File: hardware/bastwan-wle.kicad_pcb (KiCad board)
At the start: 2 copper layers, 50.8 x 22.9 mm, 34 parts, among them J1 USB_B_Micro, J2 Conn_Right, J3 Conn_Left, J4 Conn_Battery, J5 SWD, Q1 DMG3415U-7, U1 RAK3172, U2 AP2112K-3.3TRG1, U3 CP2102N-A01-GQFN28, U5 MCP73831-3-OT

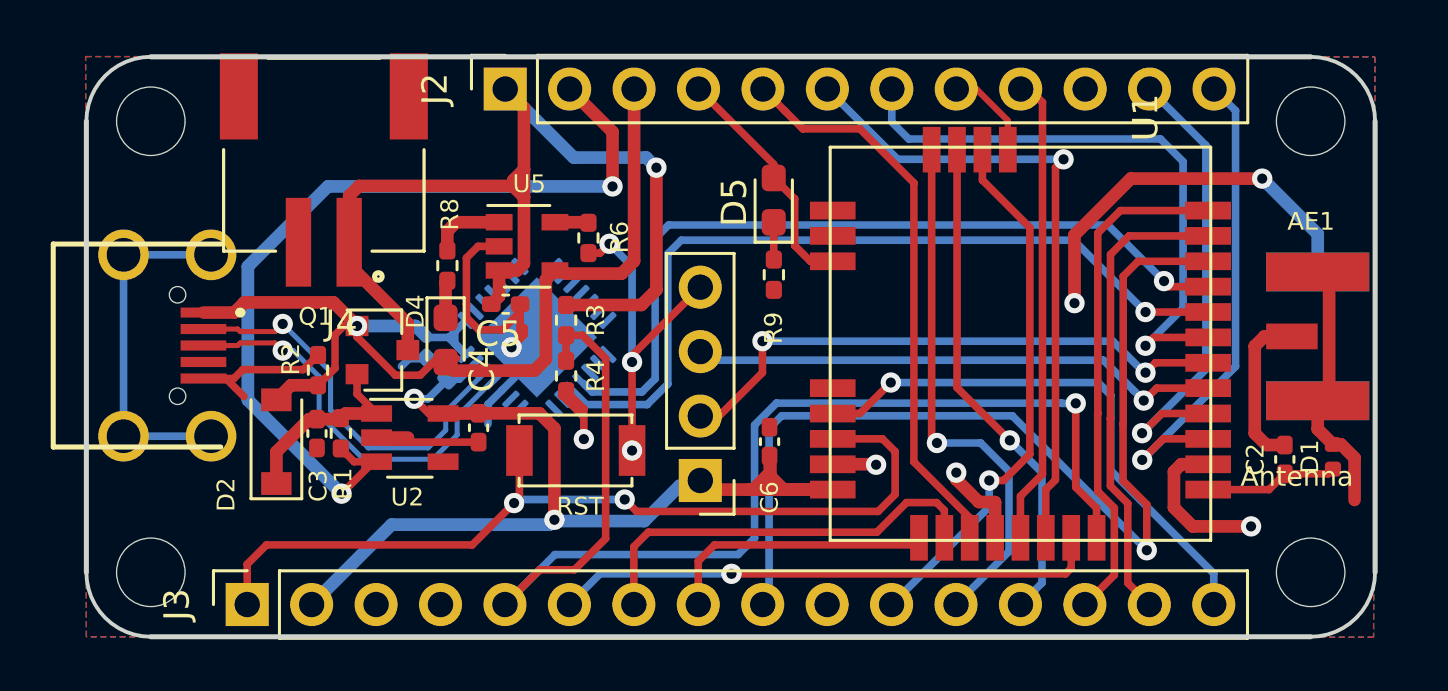
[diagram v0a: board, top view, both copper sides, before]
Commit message: fix labels
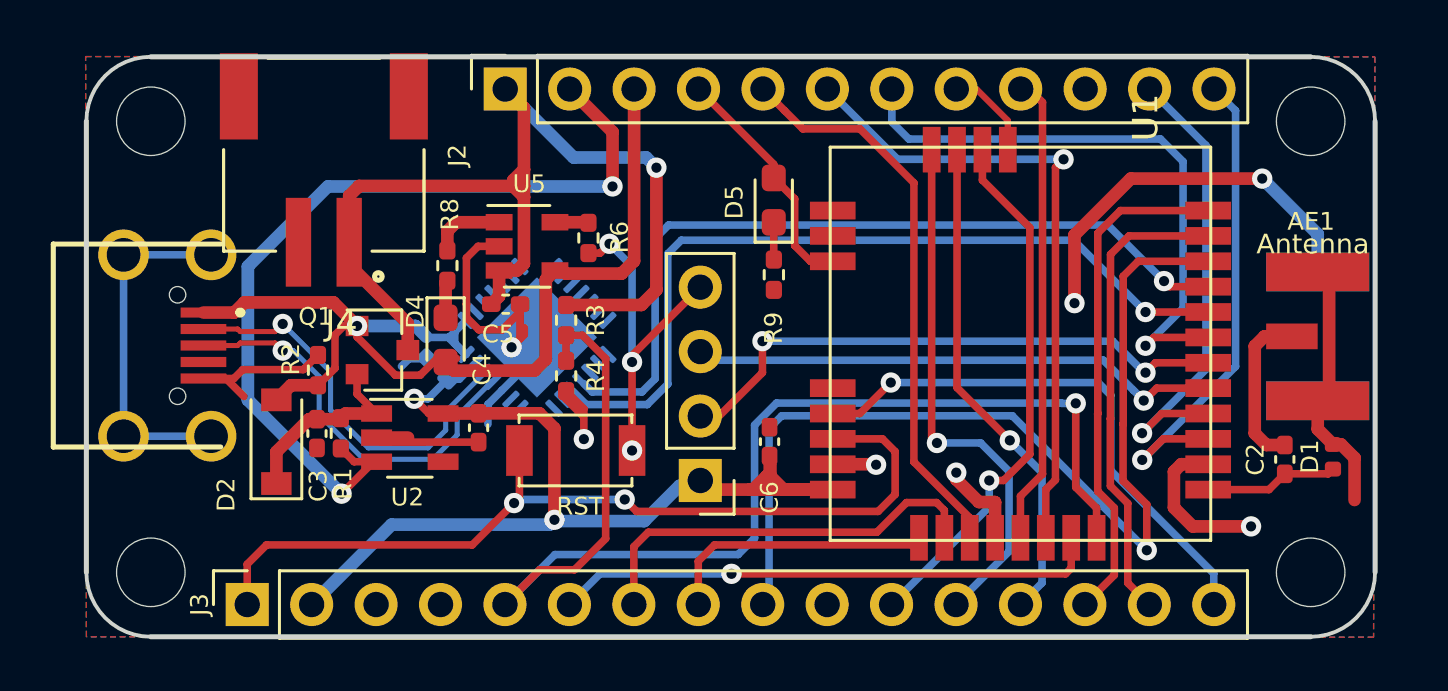
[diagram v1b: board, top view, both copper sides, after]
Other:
- board text added: "CIPO"
- board text added: "CLK"
- board text added: "COPI"
- board text removed: "AREF"
- board text removed: "MISO"
- board text removed: "MOSI"
- board text removed: "SCK"

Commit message: Last_route
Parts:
- removed R1: 100K, Resistor_SMD:R_0402_1005Metric_Pad0.72x0.64mm_HandSolder
- U2: value AP2112K-3.3TRG1 -> MCP1700_DFN6; footprint Package_TO_SOT_SMD:TSOT-23-5 -> Package_DFN_QFN:DFN-6-1EP_2x2mm_P0.65mm_EP1x1.6mm
- moved U2 1.33 mm to (125.3, 77.5)
- moved J4 0.86 mm to (124.1, 69.9)
- moved R3 0.81 mm to (133.6, 73.0)
- moved R4 0.81 mm to (133.6, 75.2)
- renumbered RST to SW1
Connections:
- J2 pad 2: /EN -> Net-(J2-Pad2)
- U2 pad 2: GND -> (no net)
- U2 pad 3: /EN -> GND
- U2 pad 5: +3V3 -> (no net)
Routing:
- net /EN: track 34.2 -> 0.00 mm, vias 2 -> 0
- net GND: track 95.5 -> 89.6 mm, vias 10 -> 16
- net /A0: track 49.1 -> 45.9 mm
- net +BATT: track 41.1 -> 39.0 mm
- net /SCL: track 18.5 -> 20.5 mm
- net /D10: track 23.9 -> 25.3 mm
- net /D6: track 18.6 -> 20.0 mm
- net /D11: track 25.7 -> 26.9 mm
- net Net-(C3-Pad1): track 7.69 -> 6.53 mm
- net +3V3: track 40.4 -> 41.4 mm
- net /SDA: track 19.4 -> 20.5 mm, vias 1 -> 2
- net /A4: track 39.1 -> 40.1 mm
- net /SWCLK: track 20.4 -> 21.1 mm
- net /SWDIO: track 22.2 -> 22.8 mm

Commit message: Add_GND
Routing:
- net GND: track 89.6 -> 84.4 mm, vias 16 -> 36
- net /D-: track 15.8 -> 14.1 mm
- net /D+: track 15.9 -> 14.3 mm
- net /RST: track 35.3 -> 34.2 mm

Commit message: Last_correction
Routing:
- net GND: track 84.4 -> 84.9 mm, vias 36 -> 37
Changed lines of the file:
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@@
     (thickness 1.6)
     (drawings 36)
-    (tracks 506)
+    (tracks 509)
     (zones 0)
     (modules 33)
@@
   (module Rf:RAK3172 (layer F.Cu)
     (at 158.22 66.22 270)
-    (fp_text reference U1 (at -1.17 2.57 90) (layer F.SilkS)
-      (effects (font (size 1 1) (thickness 0.15)))
+    (fp_text reference U1 (at 2.37 -1.62 90) (layer F.SilkS)
+      (effects (font (size 0.7 0.7) (thickness 0.1)))
     )
     (fp_text value RAK3172 (at 0.02 -2.95 90) (layer F.Fab)
@@
     (tags "resistor handsolder")
     (attr smd)
-    (fp_text reference R8 (at -2.02 -0.1 90) (layer F.SilkS)
+    (fp_text reference R8 (at 0.32 1.08 90) (layer F.SilkS)
       (effects (font (size 0.7 0.7) (thickness 0.15)))
     )
@@
   (segment (start 163.04 77.94) (end 163.36 77.94) (width 0.5) (layer F.Cu) (net 2))
   (segment (start 163.89 78.47) (end 163.89 80.13) (width 0.5) (layer F.Cu) (net 2))
-  (segment (start 162.438 69.648) (end 160.94 68.15) (width 0.5) (layer B.Cu) (net 2))
-  (segment (start 162.438 71.14) (end 162.438 69.648) (width 0.5) (layer B.Cu) (net 2))
   (segment (start 131.66 74.427107) (end 130.281142 75.805965) (width 0.3) (layer B.Cu) (net 2))
   (segment (start 131.66 73.72) (end 131.66 74.427107) (width 0.3) (layer B.Cu) (net 2))
@@
   (segment (start 124.28 78.19) (end 123.1025 78.19) (width 0.5) (layer F.Cu) (net 2))
   (via (at 151.65 72.08) (size 0.8) (drill 0.4) (layers F.Cu B.Cu) (net 2))
-  (segment (start 160.94 68.15) (end 160.25 67.46) (width 0.5) (layer B.Cu) (net 2))
-  (segment (start 160.25 67.46) (end 159.84 67.46) (width 0.5) (layer B.Cu) (net 2))
-  (segment (start 151.65 72.08) (end 151.65 70.881458) (width 0.5) (layer F.Cu) (net 2))
-  (segment (start 151.65 70.881458) (end 155.071458 67.46) (width 0.5) (layer F.Cu) (net 2))
-  (segment (start 155.071458 67.46) (end 159.84 67.46) (width 0.5) (layer F.Cu) (net 2))
   (segment (start 158.12 78.72) (end 156.89 78.72) (width 0.25) (layer F.Cu) (net 2))
   (segment (start 156.89 78.72) (end 156.51 79.1) (width 0.25) (layer F.Cu) (net 2))
@@
   (via (at 143.61 72.38) (size 0.8) (drill 0.4) (layers F.Cu B.Cu) (net 2))
   (via (at 144.64 72.38) (size 0.8) (drill 0.4) (layers F.Cu B.Cu) (net 2))
+  (segment (start 155.071458 67.46) (end 159.34 67.46) (width 0.5) (layer F.Cu) (net 2))
+  (segment (start 159.34 67.46) (end 160.05 68.17) (width 0.5) (layer F.Cu) (net 2))
+  (segment (start 151.65 70.881458) (end 155.071458 67.46) (width 0.5) (layer F.Cu) (net 2))
+  (segment (start 151.65 72.08) (end 151.65 70.881458) (width 0.5) (layer F.Cu) (net 2))
+  (segment (start 162 69.21) (end 160.34 69.21) (width 0.5) (layer B.Cu) (net 2))
+  (segment (start 162.438 71.14) (end 162.438 69.648) (width 0.5) (layer B.Cu) (net 2))
+  (segment (start 162.438 69.648) (end 162 69.21) (width 0.5) (layer B.Cu) (net 2))
+  (segment (start 160.05 68.92) (end 160.34 69.21) (width 0.5) (layer F.Cu) (net 2))
+  (segment (start 160.05 68.17) (end 160.05 68.92) (width 0.5) (layer F.Cu) (net 2))
+  (via (at 160.34 69.21) (size 0.8) (drill 0.4) (layers F.Cu B.Cu) (net 2))
   (segment (start 121.39 78.2325) (end 121.39 79.48) (width 0.5) (layer F.Cu) (net 3))
   (segment (start 122.68 76.9425) (end 121.39 78.2325) (width 0.5) (layer F.Cu) (net 3))

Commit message: Last_fix
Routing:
- net GND: track 84.9 -> 87.4 mm, vias 37 -> 38
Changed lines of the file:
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@@
     (thickness 1.6)
     (drawings 36)
-    (tracks 509)
+    (tracks 513)
     (zones 0)
     (modules 33)
@@
   (segment (start 160.05 68.17) (end 160.05 68.92) (width 0.5) (layer F.Cu) (net 2))
   (via (at 160.34 69.21) (size 0.8) (drill 0.4) (layers F.Cu B.Cu) (net 2))
+  (via (at 123.19 73.189999) (size 0.8) (drill 0.4) (layers F.Cu B.Cu) (net 2))
+  (segment (start 123.03 73.349999) (end 123.19 73.189999) (width 0.25) (layer F.Cu) (net 2))
+  (segment (start 123.03 74.4125) (end 123.03 73.349999) (width 0.25) (layer F.Cu) (net 2))
+  (segment (start 123.19 73.189999) (end 124.08 74.079999) (width 0.25) (layer B.Cu) (net 2))
   (segment (start 121.39 78.2325) (end 121.39 79.48) (width 0.5) (layer F.Cu) (net 3))
   (segment (start 122.68 76.9425) (end 121.39 78.2325) (width 0.5) (layer F.Cu) (net 3))

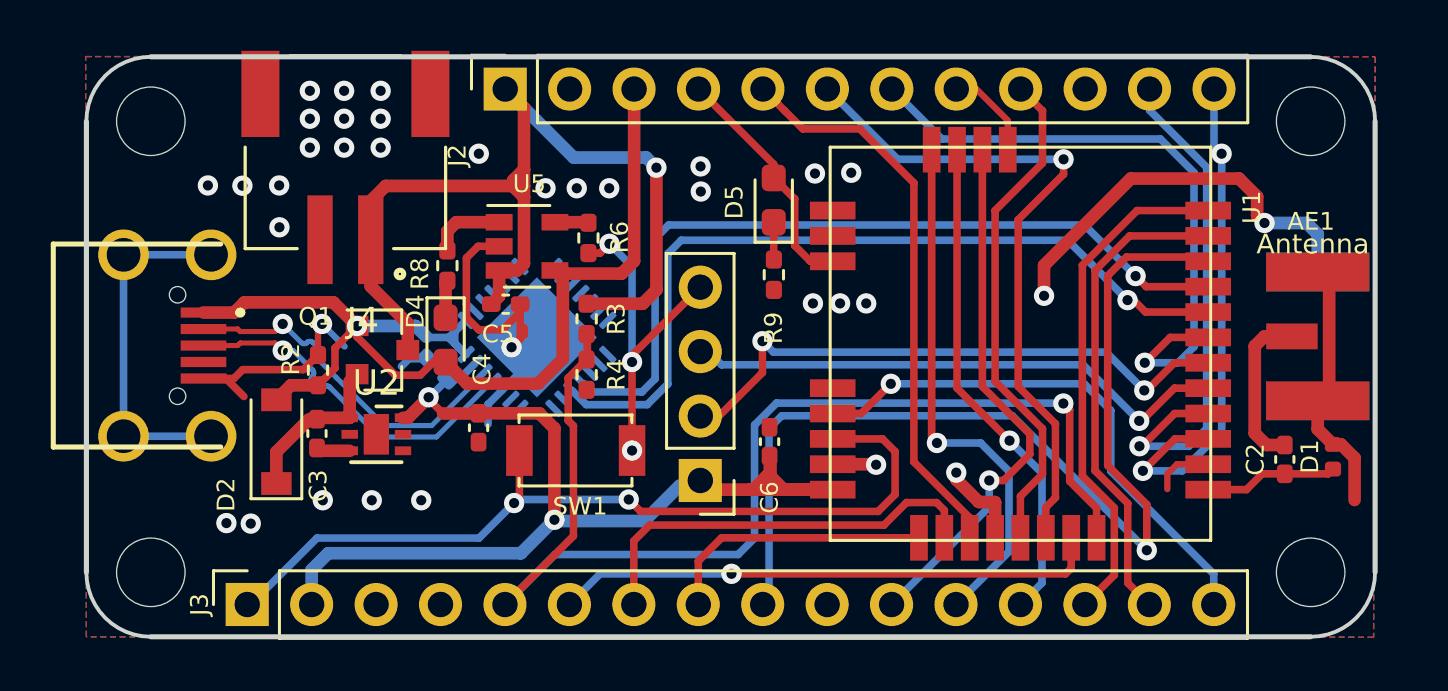
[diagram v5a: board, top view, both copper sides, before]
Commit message: Add_GND_Connection_to_Batt
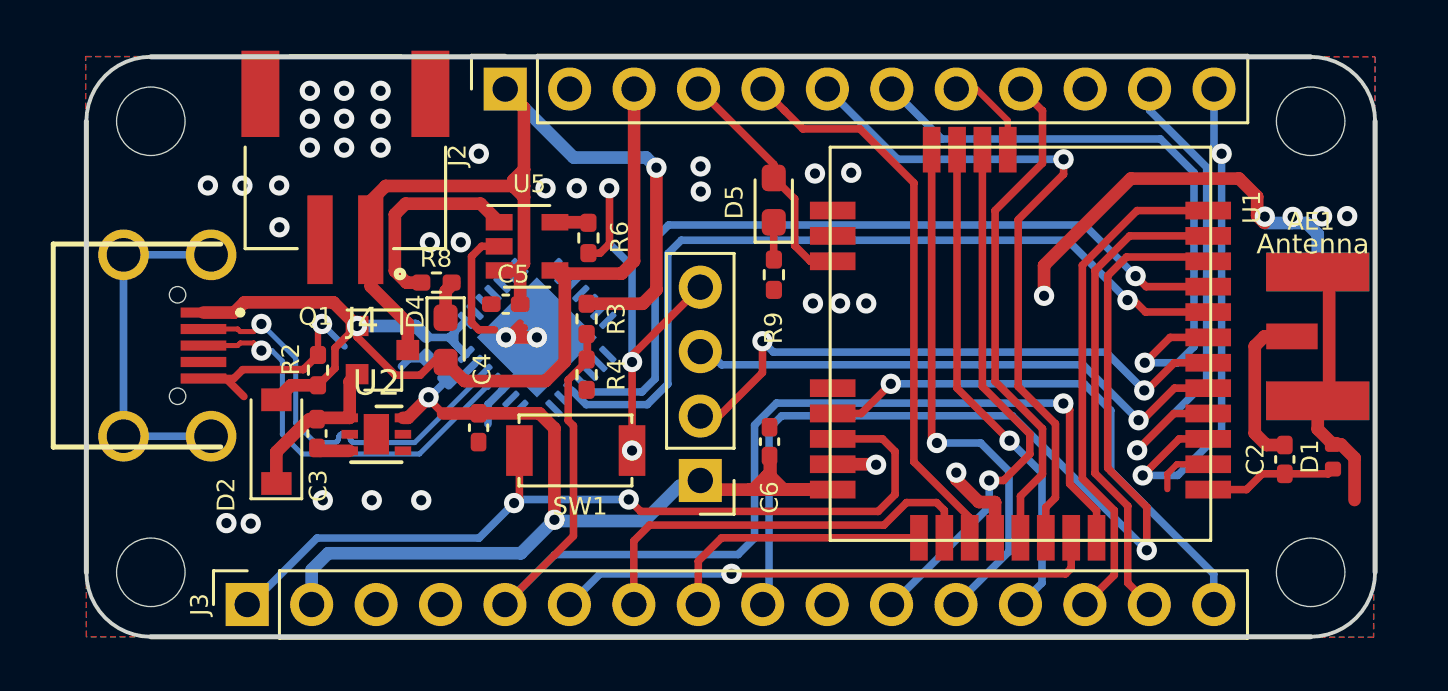
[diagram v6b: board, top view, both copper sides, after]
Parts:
- moved R8 0.80 mm to (127.7, 71.6), turned to 0 degrees
- turned C5 to 180 degrees
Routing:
- net Net-(R8-Pad1): track 2.95 -> 8.05 mm
- net /D-: track 14.1 -> 16.2 mm
- net /D+: track 14.3 -> 16.1 mm
- net /SCL: track 20.5 -> 19.7 mm
- net GND: track 87.4 -> 87.8 mm, vias 38 -> 43

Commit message: Add_connecton_to_GND
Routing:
- net GND: vias 43 -> 48
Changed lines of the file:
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@@
     (thickness 1.6)
     (drawings 36)
-    (tracks 491)
+    (tracks 499)
     (zones 0)
     (modules 33)
@@
   (segment (start 118.605 77.615) (end 115.365 77.615) (width 0.3) (layer B.Cu) (net 2))
   (segment (start 118.815 77.615) (end 118.605 77.615) (width 0.3) (layer B.Cu) (net 2))
-  (segment (start 115.365 77.615) (end 115.365 70.465) (width 0.3) (layer B.Cu) (net 2))
+  (segment (start 115.365 77.615) (end 115.365 75.255) (width 0.3) (layer B.Cu) (net 2))
   (segment (start 115.365 70.465) (end 118.815 70.465) (width 0.3) (layer B.Cu) (net 2))
   (segment (start 118.515 75.34) (end 119.4 75.34) (width 0.3) (layer F.Cu) (net 2))
@@
   (via (at 127.44 69.97) (size 0.8) (drill 0.4) (layers F.Cu B.Cu) (net 2))
   (via (at 128.66 69.97) (size 0.8) (drill 0.4) (layers F.Cu B.Cu) (net 2))
+  (segment (start 115.365 72.505) (end 115.365 70.465) (width 0.3) (layer B.Cu) (net 2))
+  (via (at 115.365 72.505) (size 0.8) (drill 0.4) (layers F.Cu B.Cu) (net 2))
+  (segment (start 115.365 73.995) (end 115.365 72.505) (width 0.3) (layer B.Cu) (net 2))
+  (via (at 115.365 73.92) (size 0.8) (drill 0.4) (layers F.Cu B.Cu) (net 2))
+  (segment (start 115.365 75.255) (end 115.365 73.995) (width 0.3) (layer B.Cu) (net 2))
+  (via (at 115.365 75.255) (size 0.8) (drill 0.4) (layers F.Cu B.Cu) (net 2))
+  (via (at 116.5 73.26) (size 0.8) (drill 0.4) (layers F.Cu B.Cu) (net 2))
+  (via (at 116.5 74.63) (size 0.8) (drill 0.4) (layers F.Cu B.Cu) (net 2))
   (segment (start 121.39 78.2325) (end 121.39 79.48) (width 0.5) (layer F.Cu) (net 3))
   (segment (start 122.68 76.9425) (end 121.39 78.2325) (width 0.5) (layer F.Cu) (net 3))

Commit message: Add_BOM_Change_footprint
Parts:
- added C7: 1uF, Capacitor_SMD:C_0402_1005Metric_Pad0.74x0.62mm_HandSolder, B.Cu at (126.2, 75.6)
- C2: footprint Capacitor_SMD:C_0402_1005Metric_Pad0.74x0.62mm_HandSolder -> Capacitor_SMD:C_0603_1608Metric_Pad1.08x0.95mm_HandSolder
- U5: value MCP73831-3-OT -> MCP73831
- moved C1 1.53 mm to (127.0, 76.3), turned to 225 degrees
- moved C2 1.03 mm to (160.2, 78.9)
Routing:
- net GND: track 87.8 -> 86.7 mm
- net Net-(AE1-Pad1): track 6.44 -> 5.68 mm
